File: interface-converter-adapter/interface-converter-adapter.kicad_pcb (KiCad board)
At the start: 2 copper layers, 61 x 38.1 mm, 6 parts, among them P1 Mezzanine-Header, P2 CONN_02X06, U1 3mm-support, U2 3mm-support, U3 3mm-support, U4 3mm-support

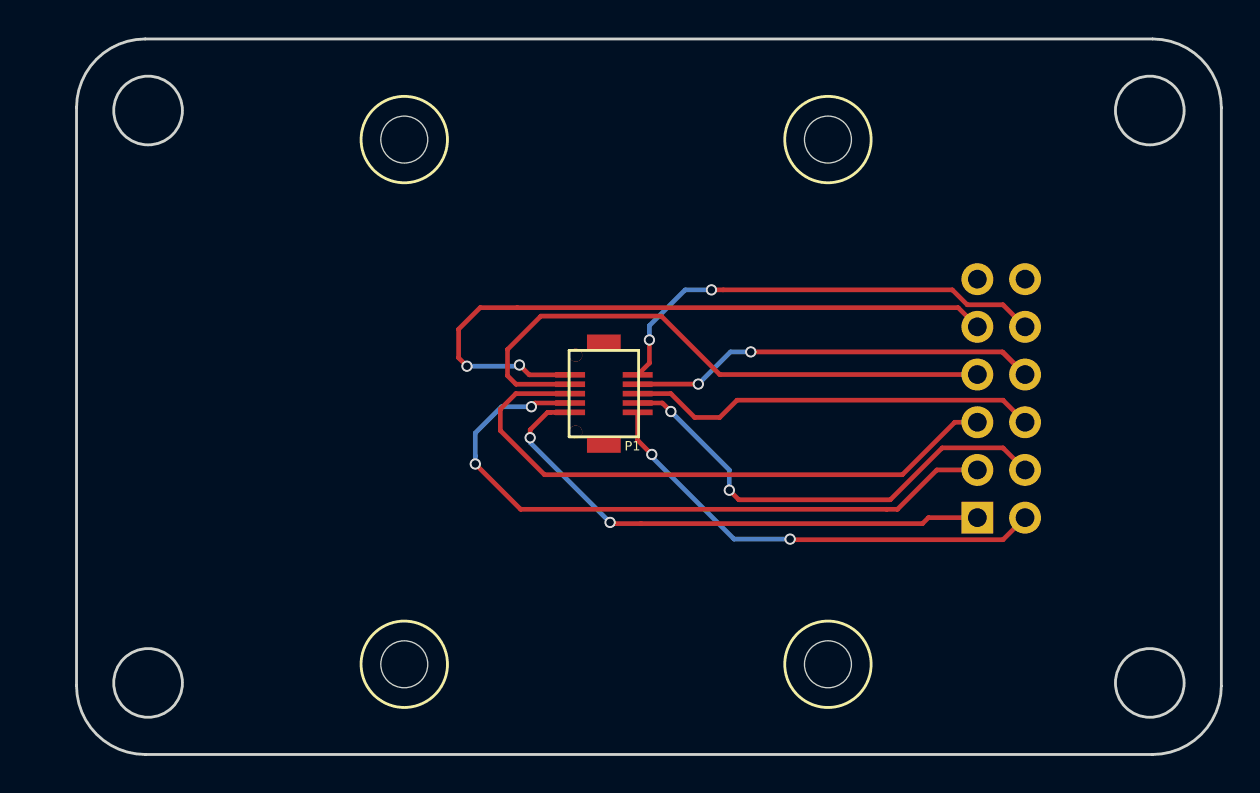
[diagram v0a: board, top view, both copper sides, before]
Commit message: Added labels and moved border slightly
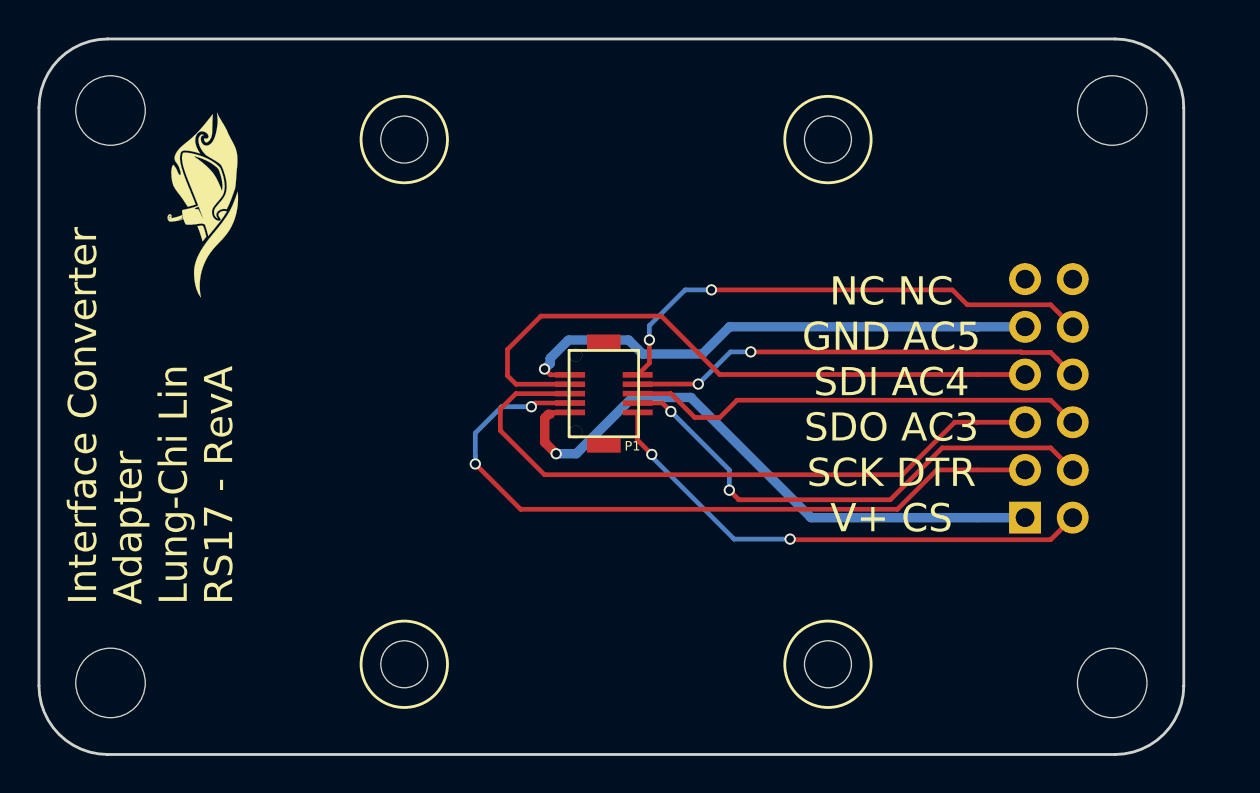
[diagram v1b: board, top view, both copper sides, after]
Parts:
- added G***: LOGO, robosub_footprints:robosub_logo-medium, F.Cu at (108.7, 90.0)
- added REF**: MountingHole_3.7mm, Mounting_Holes:MountingHole_3.7mm, F.Cu at (157.0, 85.0)
- added REF**: MountingHole_3.7mm, Mounting_Holes:MountingHole_3.7mm, F.Cu at (157.0, 115.5)
- added REF**: MountingHole_3.7mm, Mounting_Holes:MountingHole_3.7mm, F.Cu at (103.7, 115.5)
- added REF**: MountingHole_3.7mm, Mounting_Holes:MountingHole_3.7mm, F.Cu at (103.7, 85.0)
- P2: footprint Pin_Headers:Pin_Header_Angled_2x06_Pitch2.54mm -> Pin_Headers:Pin_Header_Straight_2x06_Pitch2.54mm
- moved P2 2.54 mm to (152.4, 106.7)
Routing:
- net /GND: track 36.4 -> 28.8 mm, vias 2 -> 1
- net /Vbus: track 29.7 -> 32.5 mm, vias 2 -> 1
- net /AC3: track 22.0 -> 24.6 mm
- net /TX/SCK: track 36.0 -> 38.5 mm
- net /RX/SDO: track 32.7 -> 35.3 mm
- net /DTR: track 25.0 -> 27.6 mm
- net /CS: track 24.9 -> 27.4 mm
- net /AC5: track 24.5 -> 27.0 mm
- net /SDI: track 32.0 -> 34.5 mm
- net /AC4: track 23.5 -> 24.4 mm
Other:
- outline, holes or cut-outs redrawn
- rule pad_to_mask_clearance: 0.2 -> 0
- board text added: "Interface Converter Adapter Lung-Chi Lin RS17 - RevA"
- board text added: "NC NC AC5 GND AC4 SDI AC3 SDO DTR SCK CS V+"
- board text added: "NC NC GND AC5 SDI AC4 SDO AC3 SCK DTR V+ CS"

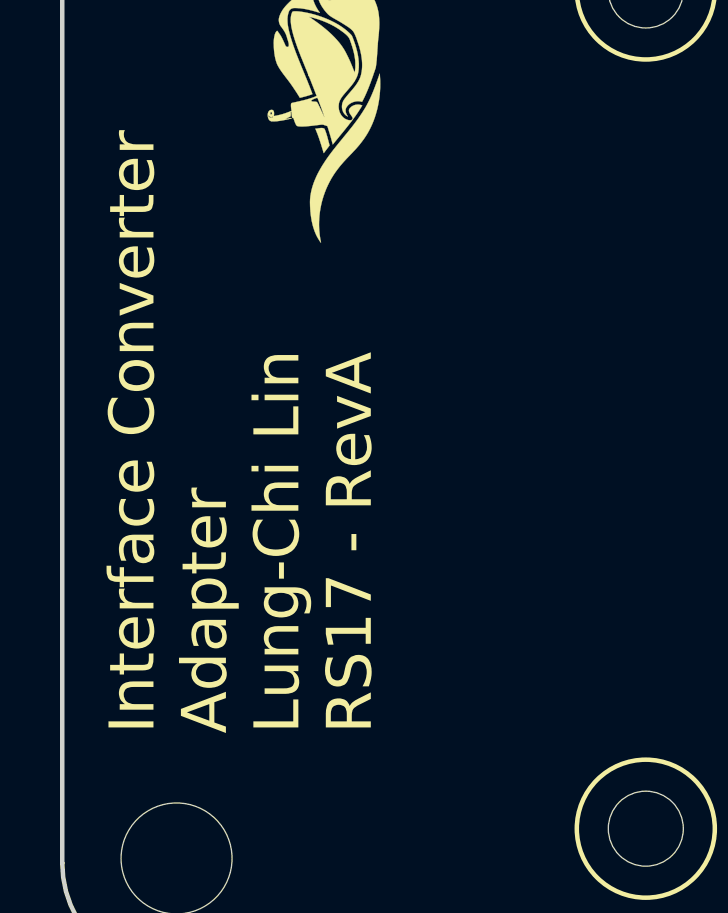
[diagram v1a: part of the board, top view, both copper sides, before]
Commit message: Corrected name on interface converter adapter
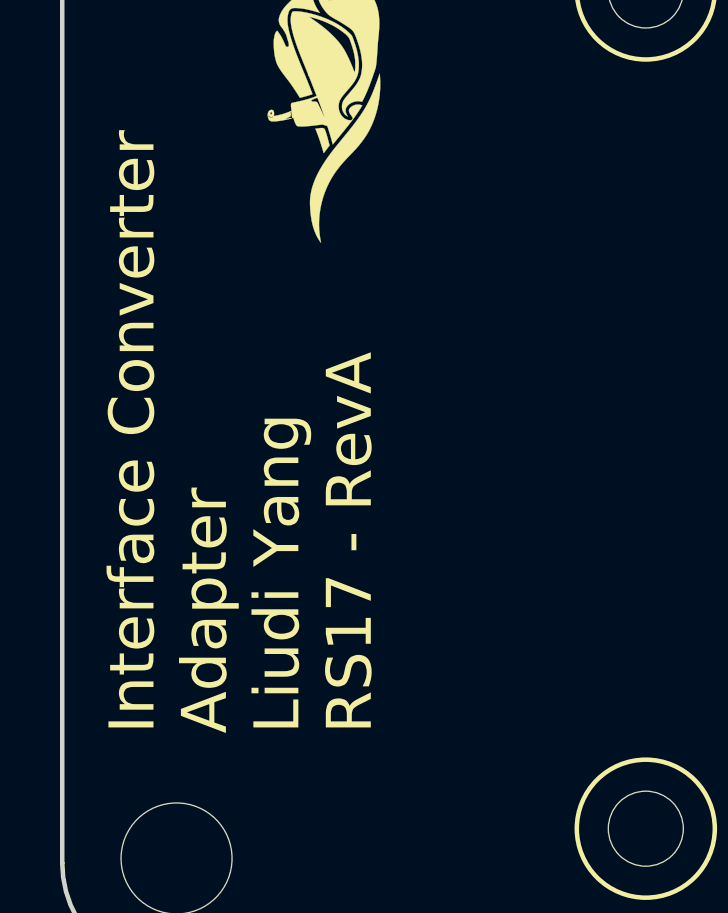
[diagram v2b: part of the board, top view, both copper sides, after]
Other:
- board text added: "Interface Converter Adapter Liudi Yang RS17 - RevA"
- board text removed: "Interface Converter Adapter Lung-Chi Lin RS17 - RevA"
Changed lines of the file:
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@@
     (links 10)
     (no_connects 0)
-    (area 101.817099 81.116099 162.927101 119.366101)
+    (area 95.573529 79.3261 165.170672 121.2561)
     (thickness 1.6)
     (drawings 11)
@@
     )
   )
-  (gr_text "Interface Converter\nAdapter\nLung-Chi Lin\nRS17 - RevA" (at 105.8611 111.3155 90) (layer F.SilkS)
+  (gr_text "Interface Converter\nAdapter\nLiudi Yang\nRS17 - RevA" (at 105.8611 111.3155 90) (layer F.SilkS)
     (effects (font (size 1.5 1.5) (thickness 0.3)) (justify left))
   )
